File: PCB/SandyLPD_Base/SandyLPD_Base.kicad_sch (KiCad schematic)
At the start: 232 parts, among them J1 Conn_02x02_Odd_Even, J10 Conn_01x10_Pin, J11 Conn_01x03, J2 Conn_01x03, J4 Conn_01x10_Pin, J5 USB_C_Receptacle_USB2.0, J6 USB_C_Receptacle_USB2.0, J7 USB_C_Receptacle_USB2.0, J8 USB_C_Receptacle_USB2.0, J9 Conn_02x02_Odd_Even, SW1 BOOT_ALT, SW2 RESET_ALT, SW3 SW_DIP_x04, SW4 BOOT_ALT, SW5 RESET_ALT, SW6 SW_DIP_x04, U1 NCP1117-3.3_SOT223, U2 NCP1117-3.3_SOT223, U3 RP2040, U4 W25Q128JVPIQ, U5 RP2040, U6 W25Q128JVPIQ, Y1 12MHz, Y2 12MHz

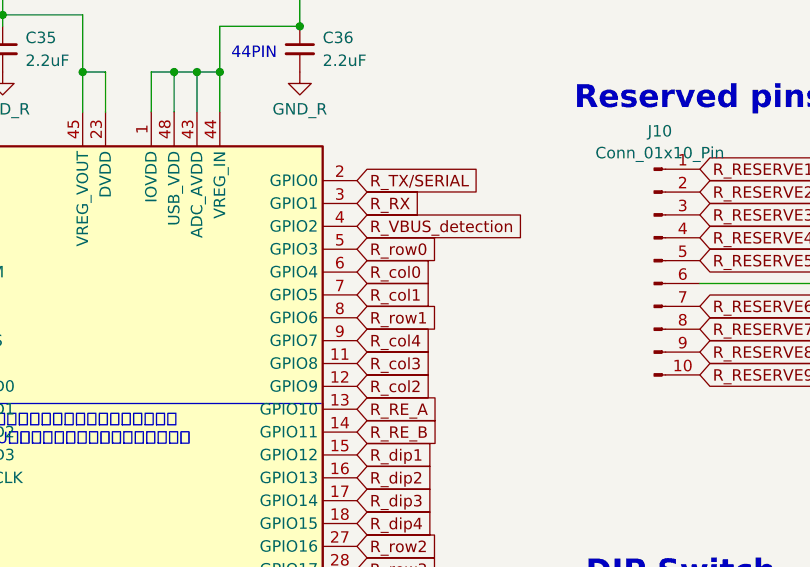
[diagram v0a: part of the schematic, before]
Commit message: 基板Base右手側　配線中
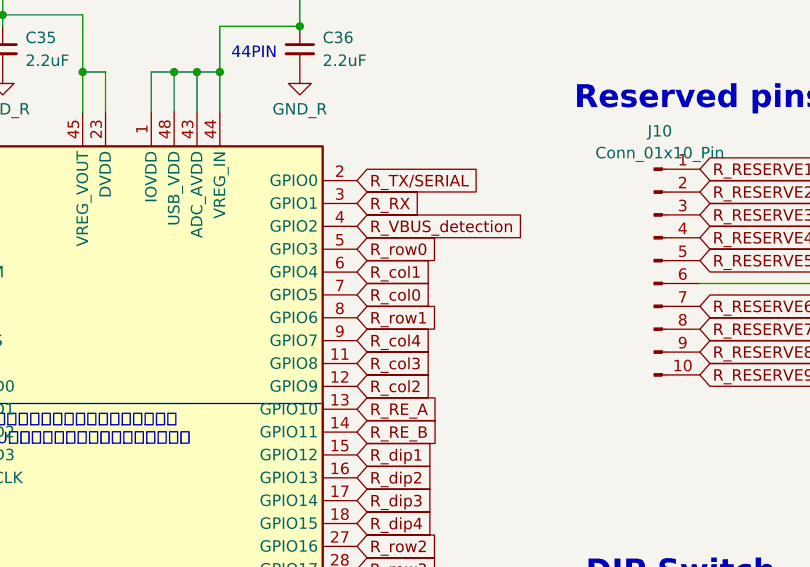
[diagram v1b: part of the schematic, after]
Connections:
- net R_col0: now also U5.7 (GPIO5); no longer U5.6 (GPIO4)
- net R_col1: now also U5.6 (GPIO4); no longer U5.7 (GPIO5)

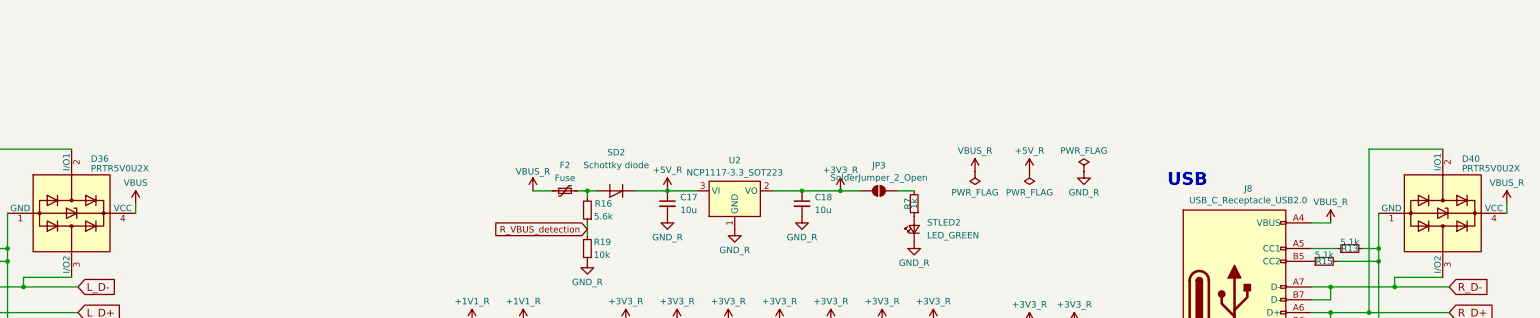
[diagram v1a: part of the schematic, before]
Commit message: シルク調整
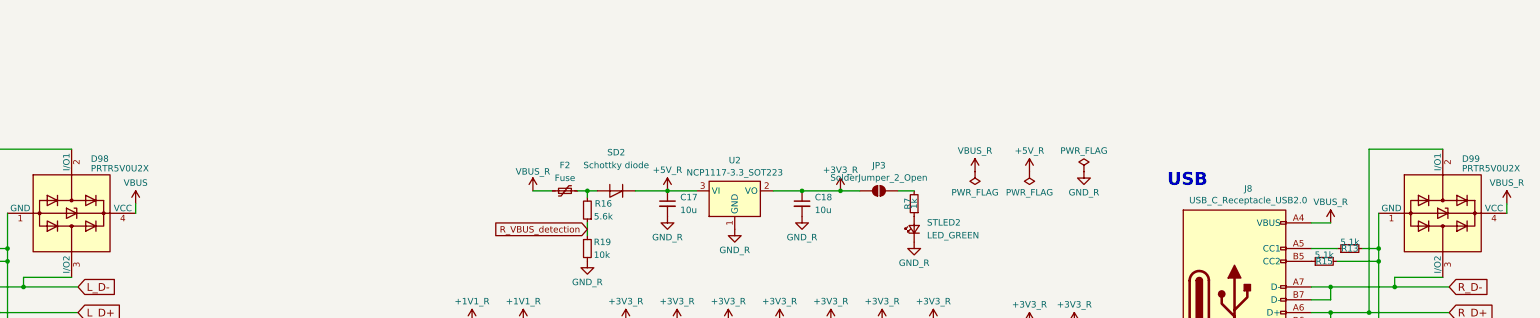
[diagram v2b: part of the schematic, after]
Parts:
- renumbered D36 to D98, D40 to D99
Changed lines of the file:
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@@
 		(on_board yes)
 		(dnp no)
-		(property "Reference" "D36"
+		(property "Reference" "D98"
 			(at 475.615 15.875 90)
 			(effects
@@
 			(project "Sandy_Base"
 				(path "/a99ab643-cdc7-4f8c-8088-c1f4faa914d1"
-					(reference "D36")
+					(reference "D98")
 					(unit 1)
 				)
@@
 		(on_board yes)
 		(dnp no)
-		(property "Reference" "D40"
+		(property "Reference" "D99"
 			(at 747.395 15.875 90)
 			(effects
@@
 			(project "SandyLPD_Base"
 				(path "/a99ab643-cdc7-4f8c-8088-c1f4faa914d1"
-					(reference "D40")
+					(reference "D99")
 					(unit 1)
 				)

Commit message: 配線ひとまず完了
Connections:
- net R_RESERVE1: now also U5.28 (GPIO17); no longer U5.29 (GPIO18)
- net R_RESERVE2: now also U5.29 (GPIO18); no longer U5.31 (GPIO20)
- net R_RESERVE3: now also U5.31 (GPIO20); no longer U5.34 (GPIO22)
- net R_RESERVE4: now also U5.34 (GPIO22); no longer U5.35 (GPIO23)
- net R_RESERVE5: now also U5.35 (GPIO23); no longer U5.36 (GPIO24)
- net R_RESERVE6: now also U5.36 (GPIO24); no longer U5.37 (GPIO25)
- net R_RESERVE7: now also U5.37 (GPIO25); no longer U5.38 (GPIO26_ADC0)
- net R_RESERVE8: now also U5.38 (GPIO26_ADC0); no longer U5.39 (GPIO27_ADC1)
- net R_RESERVE9: now also U5.39 (GPIO27_ADC1); no longer U5.40 (GPIO28_ADC2)
- net R_VBUS_detection: now also U5.41 (GPIO29_ADC3); no longer U5.4 (GPIO2)
- net R_col5: now also U5.40 (GPIO28_ADC2); no longer U5.41 (GPIO29_ADC3)
- net R_row3: now also U5.4 (GPIO2); no longer U5.28 (GPIO17)
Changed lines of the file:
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@@
 	(global_label "R_RESERVE1"
 		(shape input)
-		(at 665.48 140.97 0)
+		(at 665.48 138.43 0)
 		(fields_autoplaced yes)
 		(effects
@@
 		)
 		(property "Intersheetrefs" "${INTERSHEET_REFS}"
-			(at 679.5432 140.97 0)
+			(at 679.5432 138.43 0)
 			(effects
 				(font
@@
 	(global_label "R_row3"
 		(shape input)
-		(at 665.48 138.43 0)
+		(at 665.48 100.33 0)
 		(fields_autoplaced yes)
 		(effects
@@
 		)
 		(property "Intersheetrefs" "${INTERSHEET_REFS}"
-			(at 674.5238 138.43 0)
+			(at 674.5238 100.33 0)
 			(effects
 				(font
@@
 		)
 		(property "シート間のリファレンス" "${INTERSHEET_REFS}"
-			(at 665.48 140.2652 0)
+			(at 665.48 102.1652 0)
 			(effects
 				(font
@@
 	(global_label "R_RESERVE7"
 		(shape input)
-		(at 665.48 163.83 0)
+		(at 665.48 158.75 0)
 		(fields_autoplaced yes)
 		(effects
@@
 		)
 		(property "Intersheetrefs" "${INTERSHEET_REFS}"
-			(at 679.5432 163.83 0)
+			(at 679.5432 158.75 0)
 			(effects
 				(font
@@
 	(global_label "R_RESERVE8"
 		(shape input)
-		(at 665.48 166.37 0)
+		(at 665.48 163.83 0)
 		(fields_autoplaced yes)
 		(effects
@@
 		)
 		(property "Intersheetrefs" "${INTERSHEET_REFS}"
-			(at 679.5432 166.37 0)
+			(at 679.5432 163.83 0)
 			(effects
 				(font
@@
 	(global_label "R_RESERVE5"
 		(shape input)
-		(at 665.48 156.21 0)
+		(at 665.48 153.67 0)
 		(fields_autoplaced yes)
 		(effects
@@
 		)
 		(property "Intersheetrefs" "${INTERSHEET_REFS}"
-			(at 679.5432 156.21 0)
+			(at 679.5432 153.67 0)
 			(effects
 				(font
@@
 	(global_label "R_RESERVE6"
 		(shape input)
-		(at 665.48 158.75 0)
+		(at 665.48 156.21 0)
 		(fields_autoplaced yes)
 		(effects
@@
 		)
 		(property "Intersheetrefs" "${INTERSHEET_REFS}"
-			(at 679.5432 158.75 0)
+			(at 679.5432 156.21 0)
 			(effects
 				(font
@@
 	(global_label "R_RESERVE4"
 		(shape input)
-		(at 665.48 153.67 0)
+		(at 665.48 151.13 0)
 		(fields_autoplaced yes)
 		(effects
@@
 		)
 		(property "Intersheetrefs" "${INTERSHEET_REFS}"
-			(at 679.5432 153.67 0)
+			(at 679.5432 151.13 0)
 			(effects
 				(font
@@
 	(global_label "R_RESERVE3"
 		(shape input)
-		(at 665.48 151.13 0)
+		(at 665.48 146.05 0)
 		(fields_autoplaced yes)
 		(effects
@@
 		)
 		(property "Intersheetrefs" "${INTERSHEET_REFS}"
-			(at 679.5432 151.13 0)
+			(at 679.5432 146.05 0)
 			(effects
 				(font
@@
 	(global_label "R_RESERVE2"
 		(shape input)
-		(at 665.48 146.05 0)
+		(at 665.48 140.97 0)
 		(fields_autoplaced yes)
 		(effects
@@
 		)
 		(property "Intersheetrefs" "${INTERSHEET_REFS}"
-			(at 679.5432 146.05 0)
+			(at 679.5432 140.97 0)
 			(effects
 				(font
@@
 	(global_label "R_RESERVE9"
 		(shape input)
-		(at 665.48 168.91 0)
+		(at 665.48 166.37 0)
 		(fields_autoplaced yes)
 		(effects
@@
 		)
 		(property "Intersheetrefs" "${INTERSHEET_REFS}"
-			(at 679.5432 168.91 0)
+			(at 679.5432 166.37 0)
 			(effects
 				(font
@@
 	(global_label "R_VBUS_detection"
 		(shape input)
-		(at 665.48 100.33 0)
+		(at 665.48 171.45 0)
 		(fields_autoplaced yes)
 		(effects
@@
 		)
 		(property "Intersheetrefs" "${INTERSHEET_REFS}"
-			(at 684.6838 100.33 0)
+			(at 684.6838 171.45 0)
 			(effects
 				(font
@@
 	(global_label "R_col5"
 		(shape input)
-		(at 665.48 171.45 0)
+		(at 665.48 168.91 0)
 		(fields_autoplaced yes)
 		(effects
@@
 		)
 		(property "Intersheetrefs" "${INTERSHEET_REFS}"
-			(at 674.1609 171.45 0)
+			(at 674.1609 168.91 0)
 			(effects
 				(font
@@
 		)
 		(property "シート間のリファレンス" "${INTERSHEET_REFS}"
-			(at 665.48 173.2852 0)
+			(at 665.48 170.7452 0)
 			(effects
 				(font

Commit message: LEDをJLCPCBのBasic Partsに変更
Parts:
- STLED1, STLED2: footprint LED_SMD:LED_0603_1608Metric_Pad1.05x0.95mm_HandSolder -> LED_SMD:LED_0805_2012Metric; LCSC (none) -> C2297
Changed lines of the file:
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@@
 			)
 		)
-		(property "Footprint" "LED_SMD:LED_0603_1608Metric_Pad1.05x0.95mm_HandSolder"
+		(property "Footprint" "LED_SMD:LED_0805_2012Metric"
 			(at 367.03 29.845 90)
 			(effects
@@
 			)
 		)
-		(property "Datasheet" "https://akizukidenshi.com/catalog/g/g108275/"
+		(property "Datasheet" "https://jlcpcb.com/api/file/downloadByFileSystemAccessId/8550724011370958848"
 			(at 367.03 29.845 90)
 			(effects
@@
 			)
 		)
-		(property "LCSC" ""
+		(property "LCSC" "C2297"
 			(at 367.03 29.845 0)
 			(effects
@@
 			)
 		)
-		(property "Footprint" "LED_SMD:LED_0603_1608Metric_Pad1.05x0.95mm_HandSolder"
+		(property "Footprint" "LED_SMD:LED_0805_2012Metric"
 			(at 638.81 29.845 90)
 			(effects
@@
 			)
 		)
-		(property "Datasheet" "~"
+		(property "Datasheet" "https://jlcpcb.com/api/file/downloadByFileSystemAccessId/8550724011370958848"
 			(at 638.81 29.845 90)
 			(effects
@@
 			)
 		)
-		(property "LCSC" ""
+		(property "LCSC" "C2297"
 			(at 638.81 29.845 0)
 			(effects

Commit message: #32 DIPスイッチにLEDのON/OFFを接続
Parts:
- removed JP1, JP3: SolderJumper_2_Open, Jumper:SolderJumper-2_P1.3mm_Open_RoundedPad1.0x1.5mm, symbol Jumper:SolderJumper_2_Open
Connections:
- net +3V3: now also R1.2
- net +3V3_R: now also R7.2
- net GND: no longer J4.6 (Pin_6), STLED1.1 (K)
- net GND_R: no longer J10.6 (Pin_6), STLED2.1 (K)
- net L_RESERVE6: now also J4.6 (Pin_6); no longer J4.7 (Pin_7)
- net L_RESERVE7: now also J4.7 (Pin_7); no longer J4.8 (Pin_8)
- net L_RESERVE8: now also J4.8 (Pin_8); no longer J4.9 (Pin_9)
- net L_RESERVE9: now also J4.9 (Pin_9); no longer J4.10 (Pin_10)
- net L_dip1: now also U3.16 (GPIO13); no longer U3.15 (GPIO12)
- net L_dip2: now also U3.17 (GPIO14); no longer U3.16 (GPIO13)
- net L_dip3: now also U3.18 (GPIO15); no longer U3.17 (GPIO14)
- net R_RESERVE1: now also J10.2 (Pin_2); no longer J10.1 (Pin_1)
- net R_RESERVE2: now also J10.3 (Pin_3); no longer J10.2 (Pin_2)
- net R_RESERVE3: now also J10.4 (Pin_4); no longer J10.3 (Pin_3)
- net R_RESERVE4: now also J10.5 (Pin_5); no longer J10.4 (Pin_4)
- net R_RESERVE5: now also J10.6 (Pin_6); no longer J10.5 (Pin_5)
- net R_dip1: now also U5.16 (GPIO13); no longer U5.15 (GPIO12)
- net R_dip2: now also U5.17 (GPIO14); no longer U5.16 (GPIO13)
- net R_dip3: now also U5.18 (GPIO15); no longer U5.17 (GPIO14)
- net L_dip4 renamed PowerLED_L
- net PowerLED_L: now also STLED1.1 (K); no longer U3.18 (GPIO15)
- net R_dip4 renamed PowerLED_R
- net PowerLED_R: now also STLED2.1 (K); no longer U5.18 (GPIO15)
- new net L_RESERVE10: J4.10 (Pin_10), U3.15 (GPIO12)
- new net R_RESERVE10: J10.1 (Pin_1), U5.15 (GPIO12)
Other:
- moved on the sheet: C1, C17, C18, C2, F1, F2, R1, R12, R16, R19, R7, R8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

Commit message: シルク表示を調整
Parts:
- renumbered D17 to D10, D18 to D11, D19 to D12, D25 to D13, D26 to D14, D27 to D15, D28 to D16, D33 to D17, D3 to D18, D4 to D19, D10 to D20, D11 to D21, D12 to D22, D13 to D23, D14 to D24, D20 to D25, D21 to D26, D22 to D27, D23 to D28, D24 to D29, D5 to D3, D29 to D30, D30 to D31, D31 to D32, D32 to D33, D6 to D4, D7 to D5, D8 to D6, D9 to D7, D15 to D8, D16 to D9, H_btm_3 to H_btm_2, H_btm_4 to H_btm_3, H_btm_2 to H_btm_4, H_mid_15 to H_mid_10, H_mid_17 to H_mid_11, H_mid_4 to H_mid_12, H_mid_22 to H_mid_13, H_mid_5 to H_mid_14, H_mid_6 to H_mid_15, H_mid_7 to H_mid_16, H_mid_11 to H_mid_17, H_mid_12 to H_mid_18, H_mid_13 to H_mid_19, H_mid_14 to H_mid_20, H_mid_16 to H_mid_21, H_mid_18 to H_mid_22, H_mid_21 to H_mid_4, H_mid_19 to H_mid_5, H_mid_8 to H_mid_6, H_mid_9 to H_mid_7, H_mid_10 to H_mid_8, H_mid_20 to H_mid_9, LS4 to LS2, SW_17 to SW_10, SW_18 to SW_11, SW_19 to SW_12, SW_25 to SW_13, SW_27 to SW_14, SW_28 to SW_15, SW_29 to SW_16, SW_3 to SW_17, SW_4 to SW_18, SW_10 to SW_19, SW_11 to SW_20, SW_12 to SW_21, SW_13 to SW_22, SW_14 to SW_23, SW_20 to SW_24, SW_21 to SW_25, SW_22 to SW_26, SW_23 to SW_27, SW_24 to SW_28, SW_26 to SW_29, SW_5 to SW_3, SW_6 to SW_4, SW_7 to SW_5, SW_8 to SW_6, SW_9 to SW_7, SW_15 to SW_8, SW_16 to SW_9

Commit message: LED窓、LED位置調整
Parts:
- L1, L2, L3, L4, L5, L6: footprint LED_SMD:LED_WS2812B-2020_PLCC4_2.0x2.0mm -> locallib:LED_WS2812B-2020_PLCC4_2.0x2.0mm_with_3D_model
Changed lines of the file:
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@@
 			)
 		)
-		(property "Footprint" "LED_SMD:LED_WS2812B-2020_PLCC4_2.0x2.0mm"
+		(property "Footprint" "locallib:LED_WS2812B-2020_PLCC4_2.0x2.0mm_with_3D_model"
 			(at 364.49 233.045 0)
 			(effects
@@
 			)
 		)
-		(property "Footprint" "LED_SMD:LED_WS2812B-2020_PLCC4_2.0x2.0mm"
+		(property "Footprint" "locallib:LED_WS2812B-2020_PLCC4_2.0x2.0mm_with_3D_model"
 			(at 647.7 236.22 0)
 			(effects
@@
 			)
 		)
-		(property "Footprint" "LED_SMD:LED_WS2812B-2020_PLCC4_2.0x2.0mm"
+		(property "Footprint" "locallib:LED_WS2812B-2020_PLCC4_2.0x2.0mm_with_3D_model"
 			(at 394.97 233.045 0)
 			(effects
@@
 			)
 		)
-		(property "Footprint" "LED_SMD:LED_WS2812B-2020_PLCC4_2.0x2.0mm"
+		(property "Footprint" "locallib:LED_WS2812B-2020_PLCC4_2.0x2.0mm_with_3D_model"
 			(at 379.73 233.045 0)
 			(effects
@@
 			)
 		)
-		(property "Footprint" "LED_SMD:LED_WS2812B-2020_PLCC4_2.0x2.0mm"
+		(property "Footprint" "locallib:LED_WS2812B-2020_PLCC4_2.0x2.0mm_with_3D_model"
 			(at 632.46 236.22 0)
 			(effects
@@
 			)
 		)
-		(property "Footprint" "LED_SMD:LED_WS2812B-2020_PLCC4_2.0x2.0mm"
+		(property "Footprint" "locallib:LED_WS2812B-2020_PLCC4_2.0x2.0mm_with_3D_model"
 			(at 662.94 236.22 0)
 			(effects

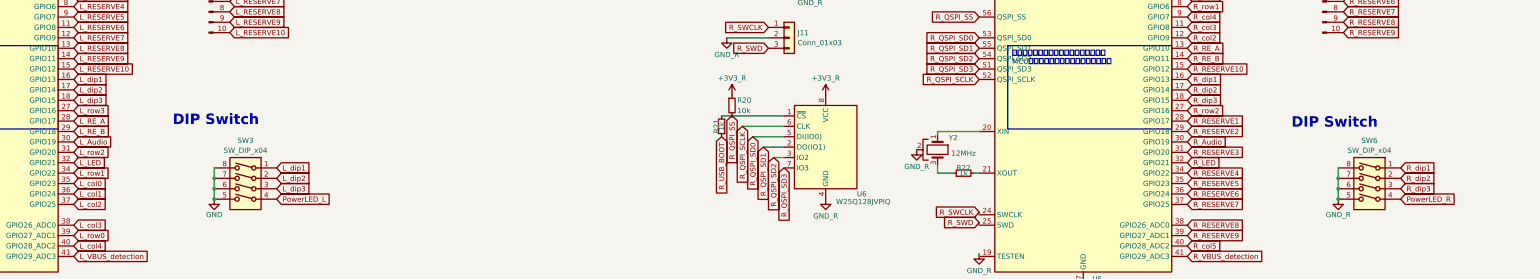
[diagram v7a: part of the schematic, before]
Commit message: DIPスイッチを調整
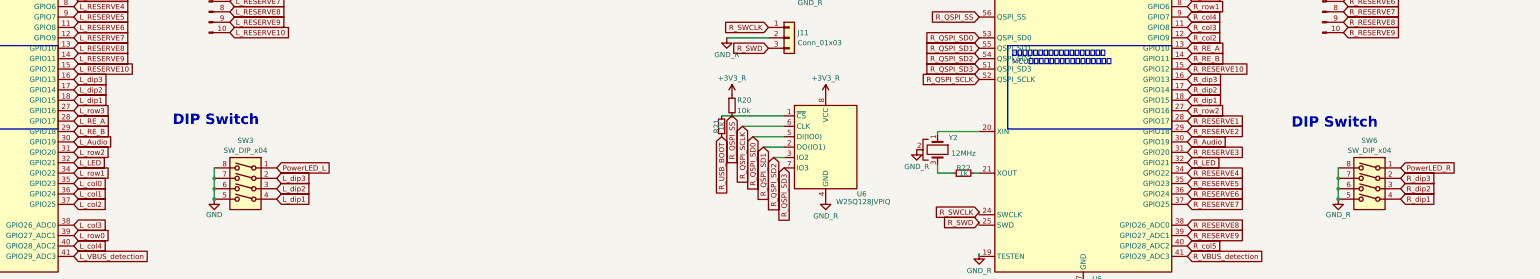
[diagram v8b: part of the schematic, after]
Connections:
- net L_dip1: now also SW3.4, U3.18 (GPIO15); no longer SW3.1, U3.16 (GPIO13)
- net L_dip2: now also SW3.3; no longer SW3.2
- net L_dip3: now also SW3.2, U3.16 (GPIO13); no longer SW3.3, U3.18 (GPIO15)
- net PowerLED_L: now also SW3.1; no longer SW3.4
- net PowerLED_R: now also SW6.1; no longer SW6.4
- net R_dip1: now also SW6.4, U5.18 (GPIO15); no longer SW6.1, U5.16 (GPIO13)
- net R_dip2: now also SW6.3; no longer SW6.2
- net R_dip3: now also SW6.2, U5.16 (GPIO13); no longer SW6.3, U5.18 (GPIO15)
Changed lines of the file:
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@@
 	(global_label "L_dip1"
 		(shape input)
-		(at 443.23 149.86 0)
+		(at 443.23 157.48 0)
 		(fields_autoplaced yes)
 		(effects
@@
 		)
 		(property "Intersheetrefs" "${INTERSHEET_REFS}"
-			(at 451.669 149.86 0)
+			(at 451.669 157.48 0)
 			(effects
 				(font
@@
 	(global_label "R_dip1"
 		(shape input)
-		(at 717.55 149.86 0)
+		(at 717.55 157.48 0)
 		(fields_autoplaced yes)
 		(effects
@@
 		)
 		(property "Intersheetrefs" "${INTERSHEET_REFS}"
-			(at 726.2309 149.86 0)
+			(at 726.2309 157.48 0)
 			(effects
 				(font
@@
 	(global_label "R_dip3"
 		(shape input)
-		(at 717.55 154.94 0)
+		(at 717.55 152.4 0)
 		(fields_autoplaced yes)
 		(effects
@@
 		)
 		(property "Intersheetrefs" "${INTERSHEET_REFS}"
-			(at 726.2309 154.94 0)
+			(at 726.2309 152.4 0)
 			(effects
 				(font
@@
 	(global_label "R_dip3"
 		(shape input)
-		(at 665.48 133.35 0)
+		(at 665.48 128.27 0)
 		(fields_autoplaced yes)
 		(effects
@@
 		)
 		(property "Intersheetrefs" "${INTERSHEET_REFS}"
-			(at 674.1609 133.35 0)
+			(at 674.1609 128.27 0)
 			(effects
 				(font
@@
 	(global_label "R_dip1"
 		(shape input)
-		(at 665.48 128.27 0)
+		(at 665.48 133.35 0)
 		(fields_autoplaced yes)
 		(effects
@@
 		)
 		(property "Intersheetrefs" "${INTERSHEET_REFS}"
-			(at 674.1609 128.27 0)
+			(at 674.1609 133.35 0)
 			(effects
 				(font
@@
 	(global_label "L_dip2"
 		(shape input)
-		(at 443.23 152.4 0)
+		(at 443.23 154.94 0)
 		(fields_autoplaced yes)
 		(effects
@@
 		)
 		(property "Intersheetrefs" "${INTERSHEET_REFS}"
-			(at 451.669 152.4 0)
+			(at 451.669 154.94 0)
 			(effects
 				(font
@@
 	(global_label "L_dip3"
 		(shape input)
-		(at 443.23 154.94 0)
+		(at 443.23 152.4 0)
 		(fields_autoplaced yes)
 		(effects
@@
 		)
 		(property "Intersheetrefs" "${INTERSHEET_REFS}"
-			(at 451.669 154.94 0)
+			(at 451.669 152.4 0)
 			(effects
 				(font
@@
 	(global_label "L_dip3"
 		(shape input)
-		(at 393.7 133.35 0)
+		(at 393.7 128.27 0)
 		(fields_autoplaced yes)
 		(effects
@@
 		)
 		(property "Intersheetrefs" "${INTERSHEET_REFS}"
-			(at 402.139 133.35 0)
+			(at 402.139 128.27 0)
 			(effects
 				(font
@@
 	(global_label "L_dip1"
 		(shape input)
-		(at 393.7 128.27 0)
+		(at 393.7 133.35 0)
 		(fields_autoplaced yes)
 		(effects
@@
 		)
 		(property "Intersheetrefs" "${INTERSHEET_REFS}"
-			(at 402.139 128.27 0)
+			(at 402.139 133.35 0)
 			(effects
 				(font
@@
 	(global_label "PowerLED_L"
 		(shape input)
-		(at 443.23 157.48 0)
+		(at 443.23 149.86 0)
 		(fields_autoplaced yes)
 		(effects
@@
 		)
 		(property "Intersheetrefs" "${INTERSHEET_REFS}"
-			(at 456.6281 157.48 0)
+			(at 456.6281 149.86 0)
 			(effects
 				(font
@@
 	(global_label "PowerLED_R"
 		(shape input)
-		(at 717.55 157.48 0)
+		(at 717.55 149.86 0)
 		(fields_autoplaced yes)
 		(effects
@@
 		)
 		(property "Intersheetrefs" "${INTERSHEET_REFS}"
-			(at 731.19 157.48 0)
+			(at 731.19 149.86 0)
 			(effects
 				(font
@@
 	(global_label "R_dip2"
 		(shape input)
-		(at 717.55 152.4 0)
+		(at 717.55 154.94 0)
 		(fields_autoplaced yes)
 		(effects
@@
 		)
 		(property "Intersheetrefs" "${INTERSHEET_REFS}"
-			(at 726.2309 152.4 0)
+			(at 726.2309 154.94 0)
 			(effects
 				(font
